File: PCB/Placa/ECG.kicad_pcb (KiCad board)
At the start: 2 copper layers, 40.6 x 23 mm, 39 parts, among them J1 Jack-stereo-gnd, P1 Bateria, P2 CONN_01X03, P3 CONN_01X03, P7 Shield, U1 INA333, U2 OPA2335, U3 OPA2335, U4 REF5050, U5 REF3112, U6 INA333, U7 OPA2335, U8 OPA2335

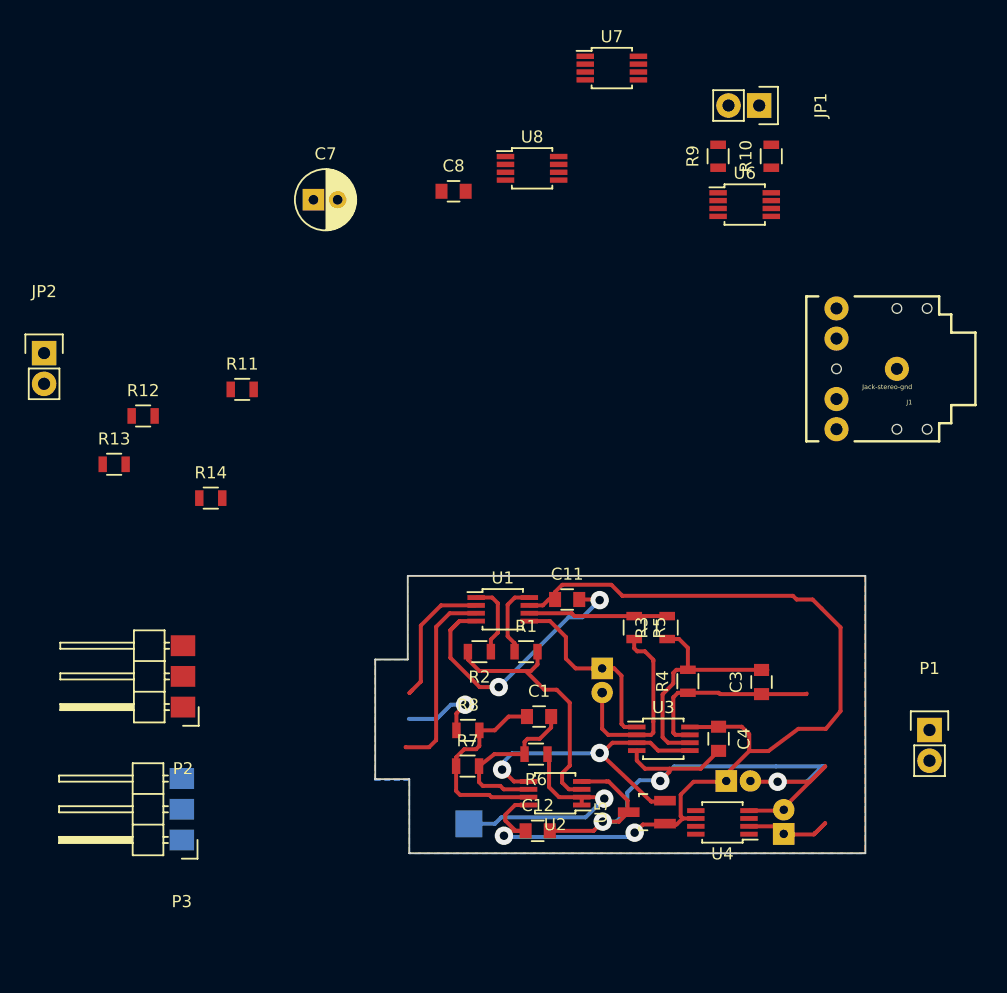
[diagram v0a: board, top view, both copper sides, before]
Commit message: Cambio el jack estéreo por un micro-USB
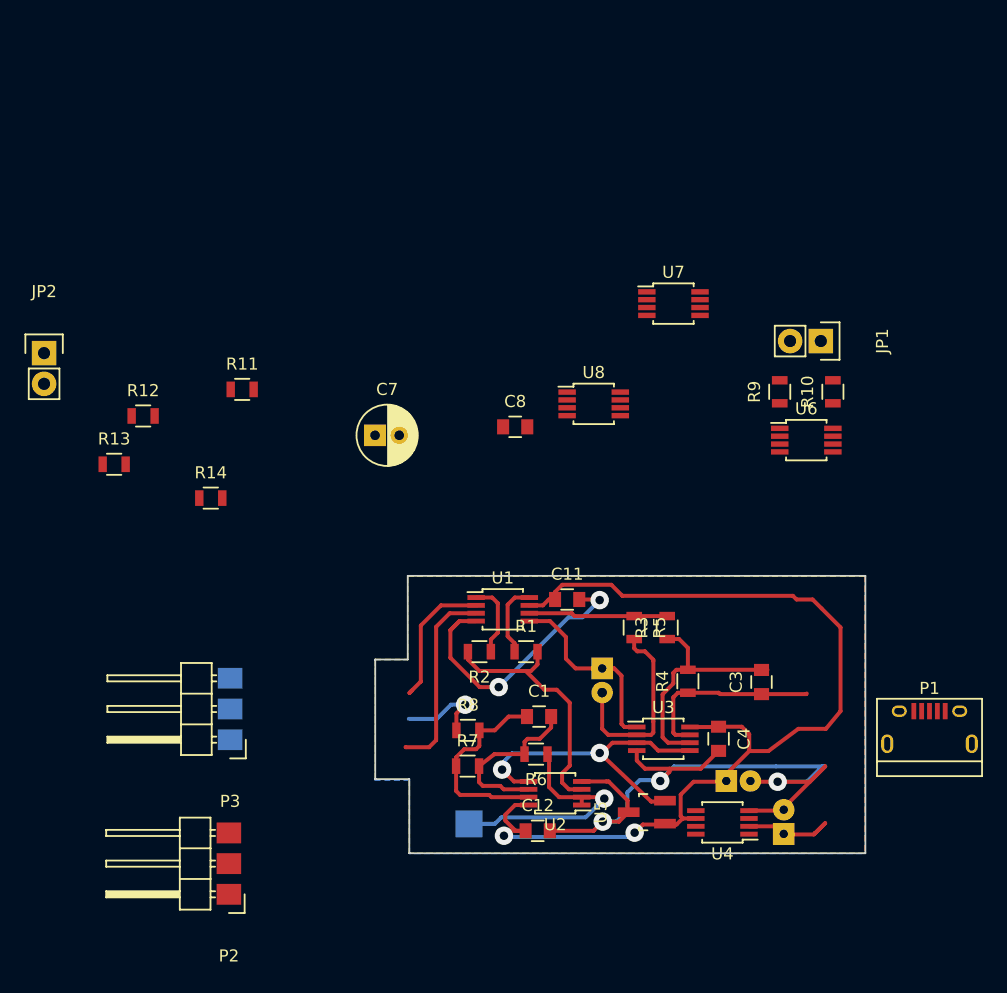
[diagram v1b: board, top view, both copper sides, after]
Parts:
- removed J1: Jack-stereo-gnd, componentes:AUDIO-JACK
- P1: value Bateria -> USB_OTG; footprint Pin_Headers:Pin_Header_Straight_1x02 -> Connect:USB_Micro-B
- moved C7 20.2 mm to (111.2, 55.9)
- moved U8 20.2 mm to (129.3, 53.3)
- moved C8 20.2 mm to (122.8, 55.2)
- moved JP1 20.2 mm to (148.1, 48.1)
- moved R10 20.2 mm to (149.1, 52.3)
- moved R9 20.2 mm to (144.7, 52.3)
- moved U6 20.2 mm to (146.9, 56.3)
- moved U7 20.2 mm to (135.9, 45.0)
- moved P2 16.0 mm to (99.1, 93.9)
- moved P3 9.21 mm to (99.2, 81.1)
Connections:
- P1 pad 1: GND -> +BATT
- P1 pad 2: +BATT -> /OUT_ch2
- P7 pad 1: SHIELD -> /SHIELD
- R12 pad 1: SHIELD -> Net-(R12-Pad1)
- R6 pad 1: SHIELD -> /SHIELD
- U2 pad 1: SHIELD -> /SHIELD
- U2 pad 2: SHIELD -> /SHIELD
- U8 pad 1: SHIELD -> Net-(R12-Pad1)
- U8 pad 2: SHIELD -> Net-(R12-Pad1)
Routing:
- net SHIELD: track 20.6 -> 0.00 mm, vias 1 -> 0
- net /SHIELD: track 0.00 -> 20.6 mm, vias 0 -> 1

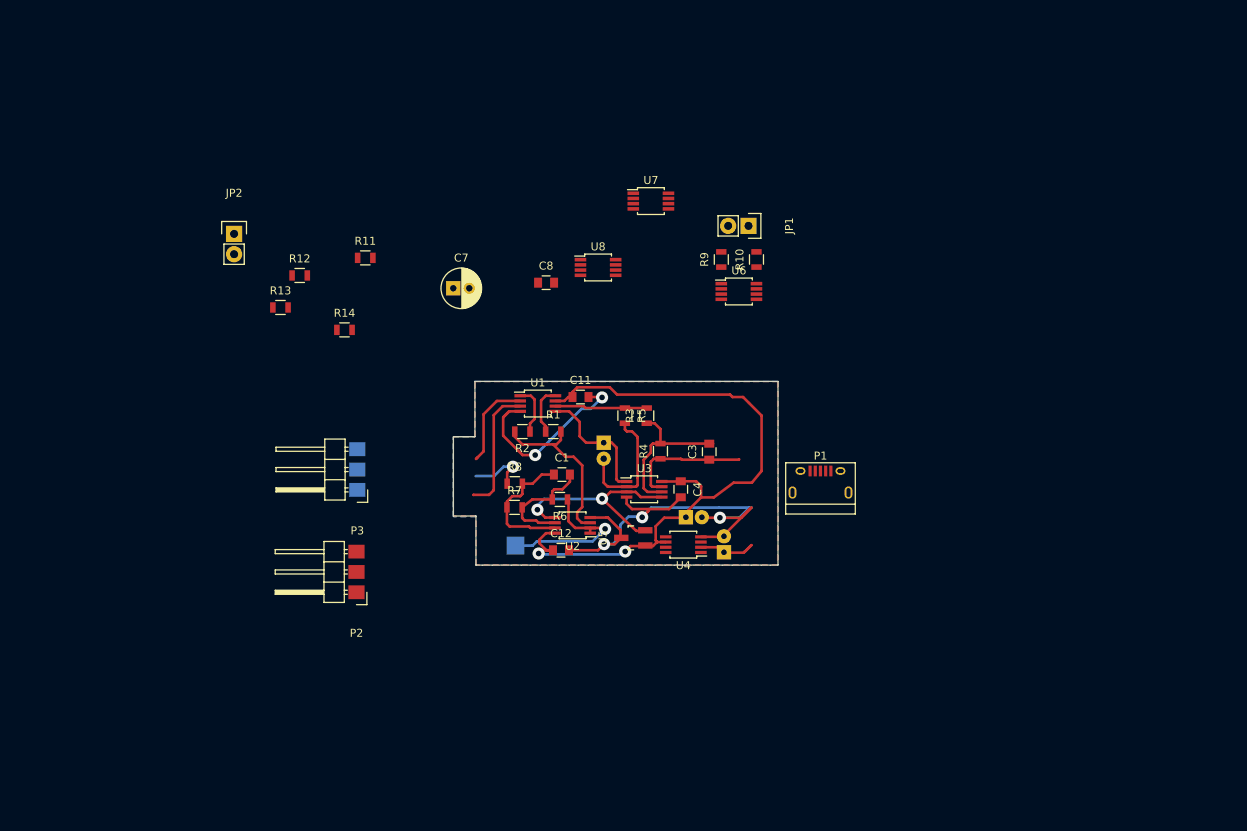
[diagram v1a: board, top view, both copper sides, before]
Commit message: Sigo con el PCB para los 2 canales.
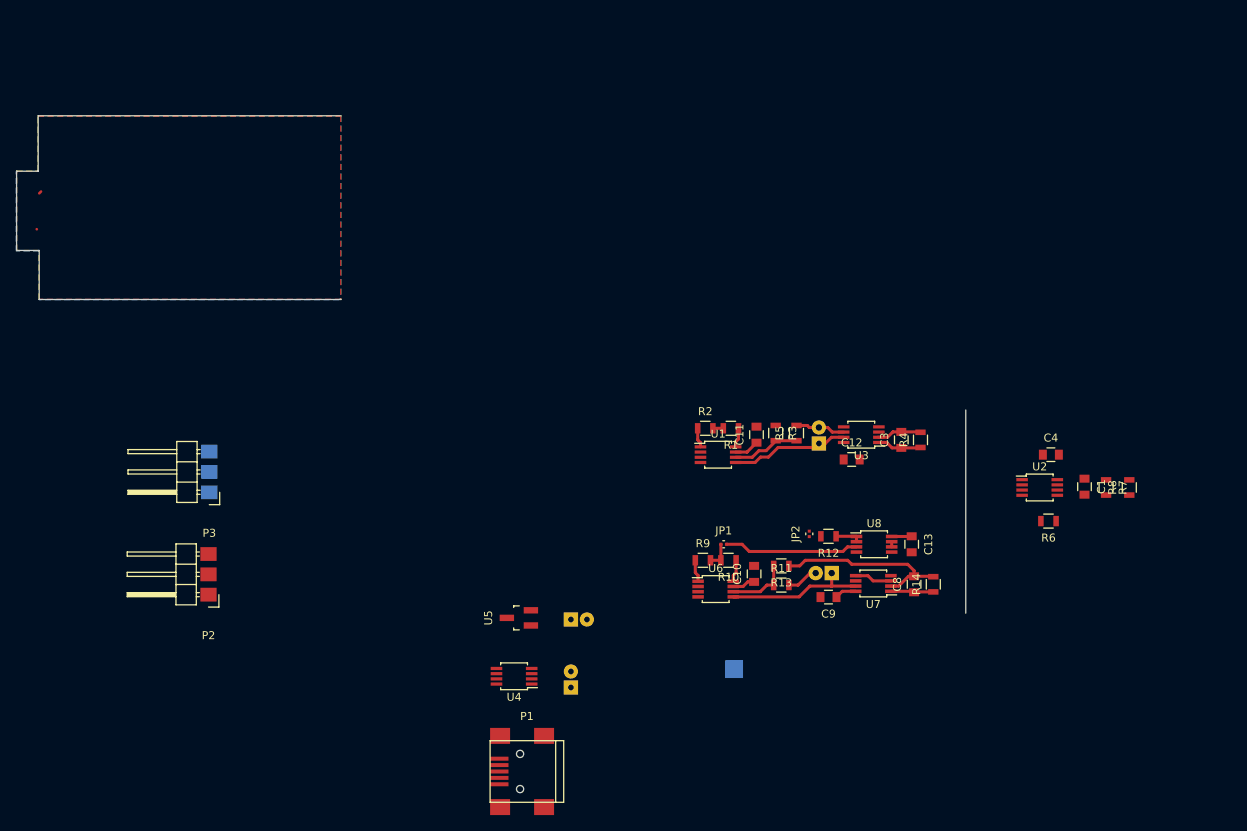
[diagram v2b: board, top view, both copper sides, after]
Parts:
- added C10: 0.1u, Capacitors_SMD:C_0805, F.Cu at (148.8, 91.6)
- added C13: 0.1u, Capacitors_SMD:C_0805, F.Cu at (168.5, 87.9)
- added C9: 0.1u, Capacitors_SMD:C_0805, F.Cu at (158.1, 94.5)
- C7: moved to B.Cu
- JP1, JP2: footprint Pin_Headers:Pin_Header_Straight_1x02 -> jumper_smd:jumper_smd
- P1: footprint Connect:USB_Micro-B -> Connect:USB_Mini-B
- moved JP2 81.1 mm to (155.7, 86.6), turned to 90 degrees
- moved R14 80.2 mm to (171.2, 92.9), turned to 90 degrees
- moved R8 76.8 mm to (195.7, 80.8), turned to 90 degrees
- moved R7 74.0 mm to (192.8, 80.8), turned to 270 degrees
- moved R12 73.7 mm to (158.1, 86.9), turned to 180 degrees
- moved R13 70.4 mm to (152.2, 90.6), turned to 180 degrees
- moved R11 66.2 mm to (152.2, 93.0)
- moved C1 65.3 mm to (190.1, 80.7), turned to 270 degrees
- moved R6 61.1 mm to (185.6, 85.0)
- moved C8 59.5 mm to (168.8, 92.9), turned to 90 degrees
- moved C7 59.2 mm to (158.5, 91.5), turned to 180 degrees
- moved U2 58.6 mm to (184.5, 80.8), turned to 0 degrees
- moved U7 55.3 mm to (163.7, 92.8), turned to 180 degrees
- moved P1 51.4 mm to (120.4, 116.3), turned to 180 degrees
- moved U8 48.9 mm to (163.8, 87.9)
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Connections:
- U3 pad 1: Net-(C2-Pad1) -> /OUT_ch1
- U3 pad 2: Net-(C2-Pad2) -> Net-(C3-Pad2)
- U3 pad 6: Net-(C3-Pad2) -> Net-(C2-Pad2)
- U3 pad 7: /OUT_ch1 -> Net-(C2-Pad1)
- U8 pad 5: (no net) -> GND
- U8 pad 6: (no net) -> Net-(U8-Pad6)
- U8 pad 7: (no net) -> Net-(U8-Pad6)
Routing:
- net GND: track 87.5 -> 0.11 mm, vias 5 -> 0
- net +5V: track 84.4 -> 11.1 mm, vias 2 -> 0
- net Net-(C8-Pad2): track 0.00 -> 23.0 mm
- net /REF: track 26.6 -> 4.67 mm, vias 2 -> 0
- net /SHIELD: track 20.6 -> 0.00 mm, vias 1 -> 0
- net Net-(R1-Pad2): track 21.5 -> 1.30 mm
- net Net-(C7-Pad1): track 0.00 -> 18.0 mm
- net Net-(C1-Pad1): track 17.8 -> 0.00 mm
- net Net-(JP1-Pad2): track 0.00 -> 16.9 mm
- net /RA_ch1: track 15.9 -> 0.00 mm
- net Net-(C3-Pad2): track 20.1 -> 5.60 mm
- net /filtro: track 14.4 -> 0.00 mm
- net /LL_ch1: track 11.6 -> 0.00 mm
- net Net-(C2-Pad2): track 16.3 -> 6.24 mm
- net /OUT_ch1: track 15.6 -> 5.60 mm
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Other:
- board size 40.6 x 23 mm -> 118.6 x 62.2 mm
- net class Default: clearance 0.1778 -> 0.2286; trace_width 0.3302 -> 0.3048; via_dia 1.524 -> 1.8
- rule trace_clearance: 0.1778 -> 0.2286
- board text added: "CH1"
- board text added: "CH2"

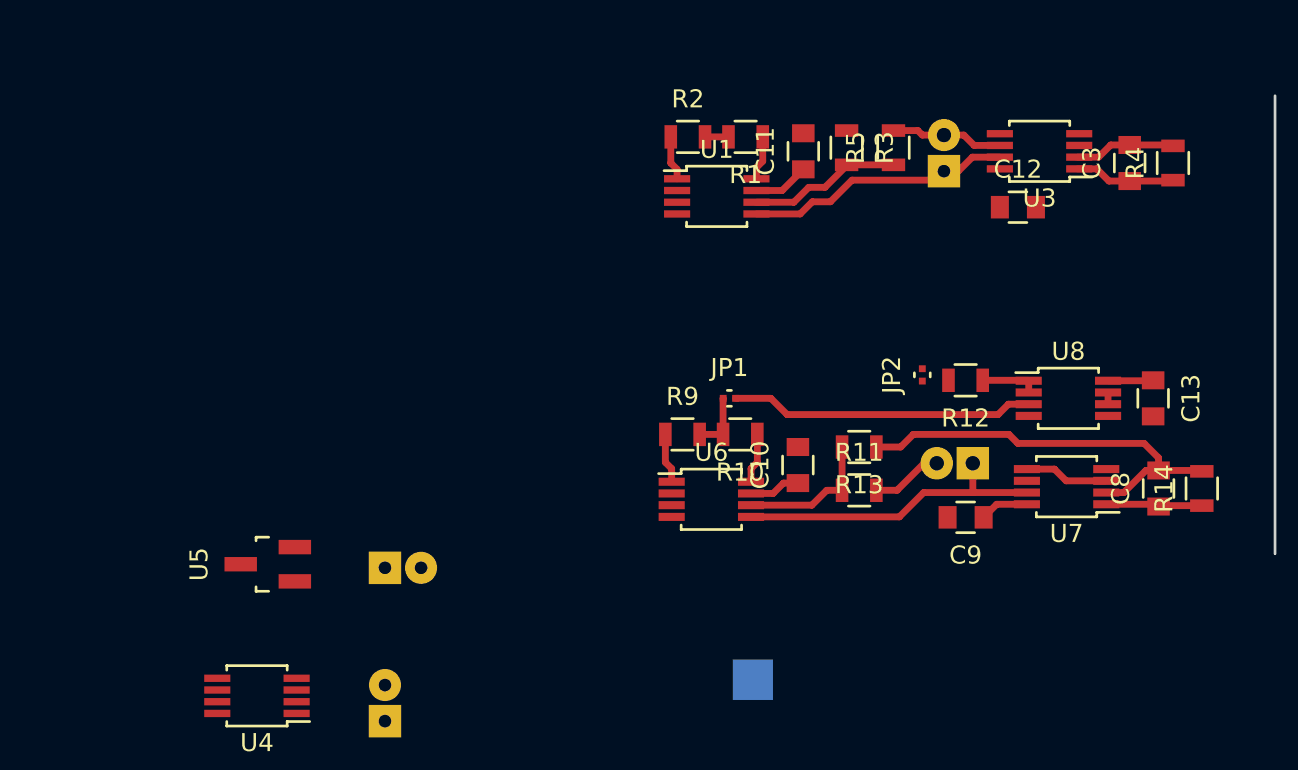
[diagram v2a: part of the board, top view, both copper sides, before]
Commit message: Actualizo el esquemático con los cambios que vi en la placa. Cambio los footprints de los capacitores C2 y C7
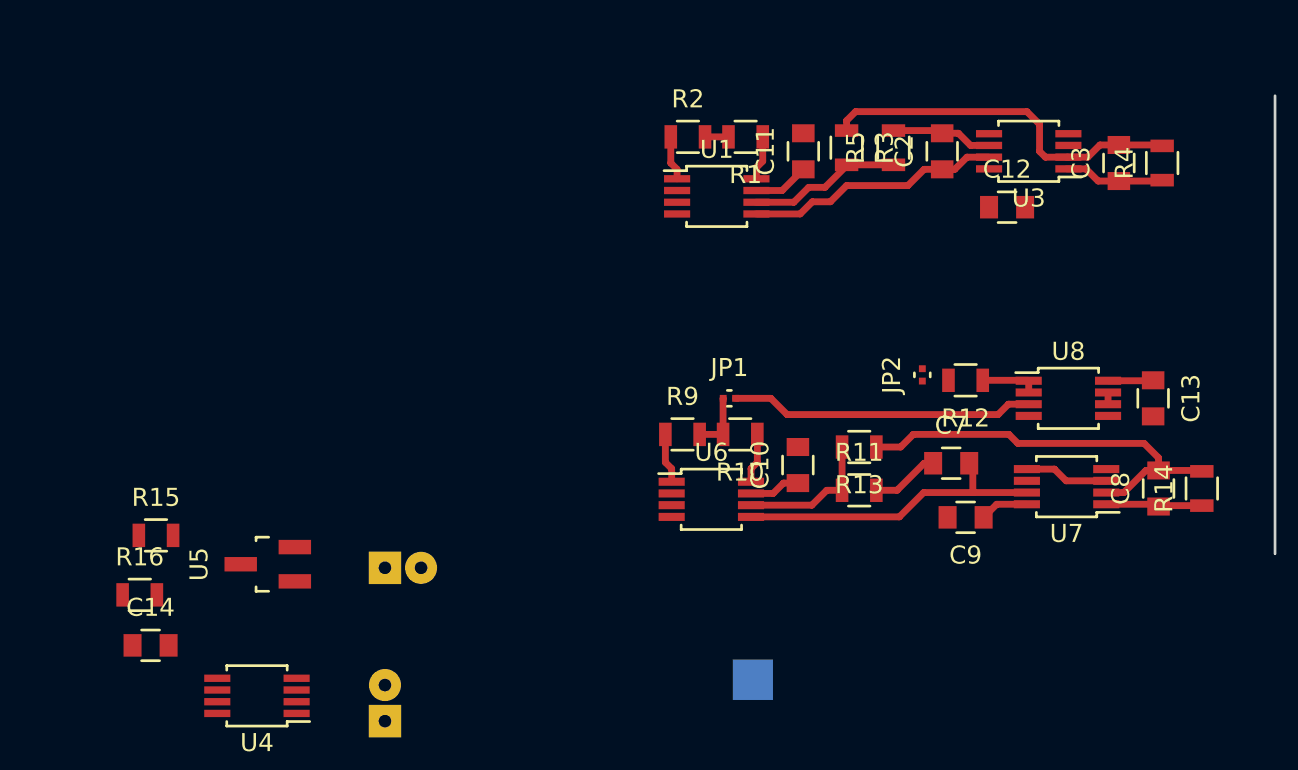
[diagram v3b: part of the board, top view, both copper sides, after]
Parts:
- added C14: 0.47u, Capacitors_SMD:C_0805, F.Cu at (112.9, 101.6)
- added R15: 4.7k, Resistors_SMD:R_0805, F.Cu at (113.2, 95.5)
- added R16: 4.7k, Resistors_SMD:R_0805, F.Cu at (112.3, 98.8)
- C2, C7: footprint Capacitors_ThroughHole:C_Radial_D5_L11_P2 -> Capacitors_SMD:C_0805; moved to F.Cu
- moved C7 1.20 mm to (157.3, 91.5), turned to 0 degrees
- moved C2 1.10 mm to (156.8, 74.2)
- moved C12 0.60 mm to (160.4, 77.3)
- moved C3 0.60 mm to (166.6, 74.8)
- moved R4 0.60 mm to (169.0, 74.8)
- moved U3 0.60 mm to (161.6, 74.2)
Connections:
- U5 pad 2: /REF -> Net-(R15-Pad2)
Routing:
- net Net-(C3-Pad2): track 5.60 -> 20.6 mm
- net Net-(C7-Pad2): track 3.97 -> 2.88 mm
- net Net-(C7-Pad1): track 18.0 -> 19.1 mm
- net Net-(C2-Pad2): track 6.24 -> 5.64 mm
- net Net-(C2-Pad1): track 14.8 -> 14.2 mm
